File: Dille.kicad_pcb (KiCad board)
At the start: 2 copper layers, 44 x 94 mm, 71 parts, among them J1 Barrel_Jack_Switch, Q1 MMBFJ112, SW2 SW_DPDT_x2, U1 PT2399, U2 TL074, U3 L78L05_SOT89

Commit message: pcb
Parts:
- removed the R5 at (79.0, 85.0)
- removed the R5 at (240.2, 79.5)
- added R5: 15k, Resistor_SMD:R_0805_2012Metric_Pad1.20x1.40mm_HandSolder, F.Cu at (51.5, 104.5)
- C14, C19, C21, C25: footprint Capacitor_SMD:CP_Elec_4x5.4 -> Capacitor_SMD:CP_Elec_4x4.5
- C2: footprint Capacitor_SMD:CP_Elec_6.3x5.4 -> Capacitor_SMD:CP_Elec_6.3x4.5; moved to F.Cu
- C20: footprint Capacitor_SMD:CP_Elec_6.3x5.4 -> Capacitor_SMD:CP_Elec_6.3x4.5
- D3, E1, RV1, RV2, RV3, SW2: moved to B.Cu
- J1: footprint Connector_BarrelJack:BarrelJack_Horizontal -> Connector_BarrelJack:BarrelJack_Kycon_KLDX-0202-xC_Horizontal; moved to B.Cu
- R11: value 10k -> 100Ω
- R13: value 15k -> 10k
- R14: value 8.2k -> 1M
- R3: value 100Ω -> 10k
- R7: value 1M -> 8.2k
- TP1: value 9V -> GND; footprint TestPoint:TestPoint_THTPad_D2.5mm_Drill1.2mm -> TestPoint:Test point 2.5x1.5
- TP2, TP3, TP4: footprint TestPoint:TestPoint_THTPad_D2.5mm_Drill1.2mm -> TestPoint:Test point 2.5x1.5
- moved C22 191.3 mm to (55.0, 102.5), turned to 180 degrees
- moved C23 190.8 mm to (55.0, 100.0), turned to 180 degrees
- moved R23 190.6 mm to (50.0, 73.0), turned to 90 degrees
- moved C26 190.0 mm to (55.0, 89.0), turned to 180 degrees
- moved C21 181.3 mm to (60.8, 89.0)
- moved R27 176.4 mm to (64.5, 81.3), turned to 180 degrees
- moved R26 176.4 mm to (64.5, 78.9)
- moved C25 174.2 mm to (72.5, 66.0), turned to 90 degrees
- moved C20 172.8 mm to (51.8, 94.5), turned to -90 degrees
- moved C24 168.4 mm to (77.0, 73.8), turned to 180 degrees
- moved R25 163.5 mm to (77.0, 81.3)
- moved R24 163.5 mm to (77.0, 78.8), turned to 180 degrees
- moved R22 160.5 mm to (80.8, 64.2), turned to 180 degrees
- moved C9 155.6 mm to (51.5, 116.5)
- moved C8 155.1 mm to (51.5, 110.5)
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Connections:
- J1 pad 1: unconnected-(J1-Pad1) -> GND
- J1 pad 2: unconnected-(J1-Pad2) -> Net-(J1-Pad2)
- R1 pad 1: Net-(R1-Pad1) -> Net-(J1-Pad2)
- R11 pad 1: Net-(C8-Pad2) -> Net-(C6-Pad2)
- R11 pad 2: Net-(C9-Pad1) -> Net-(U2A-+)
- R13 pad 1: Net-(U1-LPF1-OUT) -> Net-(U2D--)
- R13 pad 2: Net-(C9-Pad1) -> Net-(Q1-D)
- R14 pad 1: Net-(C10-Pad2) -> +4V5
- R14 pad 2: Net-(C9-Pad1) -> Net-(C6-Pad2)
- R3 pad 1: Net-(C6-Pad2) -> Net-(C8-Pad2)
- R3 pad 2: Net-(U2A-+) -> Net-(C9-Pad1)
- R7 pad 1: +4V5 -> Net-(C10-Pad2)
- R7 pad 2: Net-(C6-Pad2) -> Net-(C9-Pad1)
- TP1 pad 1: Net-(R1-Pad1) -> GND
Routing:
- net +9V: track 0.00 -> 138.9 mm
- net Net-(U1-VCO): track 0.00 -> 86.2 mm, vias 0 -> 4
- net Net-(C13-Pad2): track 0.00 -> 50.0 mm, vias 0 -> 1
- net Net-(C9-Pad1): track 0.00 -> 48.7 mm
- net Net-(Q1-D): track 3.97 -> 45.4 mm, vias 0 -> 2
- net Net-(R15-Pad1): track 0.00 -> 41.2 mm, vias 0 -> 2
- net +4V5: track 0.00 -> 38.8 mm, vias 0 -> 2
- net +5V: track 0.00 -> 36.4 mm, vias 0 -> 2
- net Net-(C25-Pad2): track 0.00 -> 34.3 mm
- net Net-(C10-Pad2): track 0.00 -> 28.1 mm, vias 0 -> 2
- net Net-(U1-LPF1-OUT): track 0.00 -> 24.3 mm
- net Net-(U1-OP2-OUT): track 0.00 -> 20.6 mm
- net Net-(SW2A-B): track 0.00 -> 16.3 mm
- net Net-(U1-LPF2-OUT): track 0.00 -> 15.7 mm
- net Net-(U2A-+): track 0.00 -> 15.1 mm, vias 0 -> 2
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- added copper zone on B.Cu, net GND
- added copper zone on F.Cu, net GND
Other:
- board size 44 x 94 mm -> 44 x 95.5 mm
- board text added: "+ 9V -"
- board text added: "LED"

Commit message: pcb 2
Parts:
- moved R22 29.8 mm to (51.0, 63.2)
- moved RV2 27.9 mm to (83.0, 67.3)
- moved RV3 27.9 mm to (55.1, 67.3)
- moved R1 11.5 mm to (84.5, 58.0), turned to 180 degrees
- moved D1 11.1 mm to (84.5, 60.5), turned to 0 degrees
- moved R2 5.68 mm to (77.5, 58.0)
- moved C5 5.57 mm to (77.5, 63.0)
- moved R4 5.57 mm to (77.5, 60.5)
- moved R23 1.12 mm to (50.5, 74.0), turned to 180 degrees
- moved C13 0.50 mm to (84.0, 84.0), turned to 0 degrees
- moved R15 0.50 mm to (84.0, 86.5)
- moved R16 0.50 mm to (84.0, 89.0)
- moved TP2 0.22 mm to (88.0, 79.8)
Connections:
- net Net-(C25-Pad2) renamed Sig out
- net Net-(C6-Pad1) renamed Sig in
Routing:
- net Net-(U1-VCO): track 86.2 -> 54.4 mm, vias 4 -> 3
- net Net-(C13-Pad2): track 50.0 -> 29.2 mm, vias 1 -> 2
- net Net-(J1-Pad2): track 9.15 -> 21.4 mm
- net +4V5: track 38.8 -> 32.7 mm
- net +9V: track 138.9 -> 133.6 mm
- net Net-(C19-Pad2): track 13.2 -> 18.1 mm, vias 0 -> 1
- net Net-(R22-Pad2): track 8.17 -> 9.18 mm
- net Net-(R15-Pad1): track 41.2 -> 41.7 mm
- net GND: vias 25 -> 36

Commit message: Saddamointi
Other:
- board text added: "https://github.com/ Secret624/Dille"

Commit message: Added gerbers
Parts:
- added REF**: Pin_D0.7mm_L6.5mm_W1.8mm_FlatFork, Connector_Pin:Pin_D0.7mm_L6.5mm_W1.8mm_FlatFork, B.Cu at (36.0, 97.0)
- added REF**: Pin_D0.7mm_L6.5mm_W1.8mm_FlatFork, Connector_Pin:Pin_D0.7mm_L6.5mm_W1.8mm_FlatFork, B.Cu at (102.0, 97.0)
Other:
- board text added: "JLCJLCJLCJLC"

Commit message: Rev 2
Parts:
- moved R22 0.50 mm to (51.0, 63.8)
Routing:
- net Net-(SW2A-B): track 16.3 -> 17.6 mm
- net +9V: track 133.6 -> 132.8 mm
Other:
- board text added: "rev. 2"
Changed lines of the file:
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@@
   )
   (footprint "Resistor_SMD:R_0805_2012Metric_Pad1.20x1.40mm_HandSolder" (layer "F.Cu")
-    (at 51 63.25 180)
+    (at 51 63.75 180)
     (descr "Resistor SMD 0805 (2012 Metric), square (rectangular) end terminal, IPC_7351 nominal with elongated pad for handsoldering. (Body size source: IPC-SM-782 page 72, https://www.pcb-3d.com/wordpress/wp-content/uploads/ipc-sm-782a_amendment_1_and_2.pdf), generated with kicad-footprint-generator")
     (tags "resistor handsolder")
@@
     (fp_circle (center 0 0) (end 0 6.1)
       (stroke (width 0.1) (type default)) (fill none) (layer "Dwgs.User"))
-    (pad "1" thru_hole circle (at -6.05 7.1) (size 2.5 2.5) (drill 1.3) (layers "*.Cu" "*.Mask")
+    (pad "1" thru_hole oval (at -5.25 7.1) (size 5.5 3) (drill oval 4 1.5) (layers "*.Cu" "*.Mask")
       (net 3 "GND") (pinfunction "A") (pintype "passive"))
-    (pad "2" thru_hole circle (at -6.05 0) (size 2.5 2.5) (drill 1.3) (layers "*.Cu" "*.Mask")
+    (pad "2" thru_hole oval (at -5.25 0) (size 5.5 3) (drill oval 4 1.5) (layers "*.Cu" "*.Mask")
       (net 37 "Net-(SW2A-B)") (pinfunction "B") (pintype "passive"))
-    (pad "3" thru_hole circle (at -6.05 -7.1) (size 2.5 2.5) (drill 1.3) (layers "*.Cu" "*.Mask")
+    (pad "3" thru_hole oval (at -5.25 -7.1) (size 5.5 3) (drill oval 4 2) (layers "*.Cu" "*.Mask")
       (net 2 "+9V") (pinfunction "C") (pintype "passive"))
-    (pad "4" thru_hole circle (at 6.05 -7.1) (size 2.5 2.5) (drill 1.3) (layers "*.Cu" "*.Mask")
+    (pad "4" thru_hole oval (at 5.25 -7.1) (size 5.5 3) (drill oval 4 2) (layers "*.Cu" "*.Mask")
       (net 15 "unconnected-(SW2B-A-Pad4)") (pinfunction "A") (pintype "passive+no_connect"))
-    (pad "5" thru_hole circle (at 6.05 0) (size 2.5 2.5) (drill 1.3) (layers "*.Cu" "*.Mask")
+    (pad "5" thru_hole oval (at 5.25 0) (size 5.5 3) (drill oval 4 2) (layers "*.Cu" "*.Mask")
       (net 16 "unconnected-(SW2B-B-Pad5)") (pinfunction "B") (pintype "passive+no_connect"))
-    (pad "6" thru_hole circle (at 6.05 7.1) (size 2.5 2.5) (drill 1.3) (layers "*.Cu" "*.Mask")
+    (pad "6" thru_hole oval (at 5.25 7.1) (size 5.5 3) (drill oval 4 1.5) (layers "*.Cu" "*.Mask")
       (net 17 "unconnected-(SW2B-C-Pad6)") (pinfunction "C") (pintype "passive+no_connect"))
     (model "${KIPRJMOD}/stepsis/SF17010F-0302-21R-L.step"
@@
       (rotate (xyz 0 0 0))
     )
-    (model "${KIPRJMOD}/Resources/SF17010F-0302-21R-L.step"
-      (offset (xyz 0 0 3))
-      (scale (xyz 1 1 1))
-      (rotate (xyz 0 0 0))
-    )
-    (model "C:/Users/Uusi/Documents/KiCad/7.0/3dmodels/SF17010F-0302-21R-L.step"
-      (offset (xyz 0 0 3))
-      (scale (xyz 1 1 1))
-      (rotate (xyz 0 0 0))
-    )
   )
   (footprint "Potentiometer_THT:UT right angle long pin" (layer "B.Cu")
@@
     (effects (font (size 1 1) (thickness 0.16) bold) (justify left bottom))
   )
+  (gr_text "rev. 2" (at 49 62.5) (layer "F.SilkS")
+    (effects (font (size 1.5 1.5) (thickness 0.3) bold) (justify left bottom))
+  )
   (gr_text "LED" (at 69 108.5) (layer "F.SilkS")
     (effects (font (size 1 1) (thickness 0.15)))
@@
   (segment (start 70.75 78.171472) (end 69.078528 76.5) (width 0.5) (layer "F.Cu") (net 2))
   (segment (start 90 65) (end 90 98) (width 0.5) (layer "F.Cu") (net 2))
-  (segment (start 62.95 109.26) (end 64.94 111.25) (width 0.25) (layer "F.Cu") (net 2))
-  (segment (start 83.1 60.5) (end 83.1 58.15) (width 1) (layer "F.Cu") (net 2))
   (segment (start 80.5 108.5) (end 80.5 100) (width 0.25) (layer "F.Cu") (net 2))
+  (segment (start 83.1 60.5) (end 83.1 58.15) (width 1) (layer "F.Cu") (net 2))
+  (segment (start 63.75 109.26) (end 65.74 111.25) (width 0.25) (layer "F.Cu") (net 2))
   (segment (start 63.475 78.3475) (end 65.5125 76.31) (width 0.25) (layer "F.Cu") (net 2))
   (segment (start 69.078528 76.5) (end 68.525 76.5) (width 0.5) (layer "F.Cu") (net 2))
+  (segment (start 65.74 111.25) (end 77.75 111.25) (width 0.25) (layer "F.Cu") (net 2))
   (segment (start 72 82.75) (end 70.75 81.5) (width 0.5) (layer "F.Cu") (net 2))
   (segment (start 89 64) (end 90 65) (width 0.5) (layer "F.Cu") (net 2))
@@
   (segment (start 79.81 78.81) (end 77.975 78.81) (width 0.25) (layer "F.Cu") (net 2))
   (segment (start 68.525 76.5) (end 65.7025 76.5) (width 0.5) (layer "F.Cu") (net 2))
-  (segment (start 80.5 100) (end 82.5 100) (width 0.25) (layer "F.Cu") (net 2))
-  (segment (start 90 98) (end 88 100) (width 0.5) (layer "F.Cu") (net 2))
   (segment (start 77.75 111.25) (end 80.5 108.5) (width 0.25) (layer "F.Cu") (net 2))
-  (segment (start 64.94 111.25) (end 77.75 111.25) (width 0.25) (layer "F.Cu") (net 2))
+  (segment (start 90 98) (end 88 100) (width 0.5) (layer "F.Cu") (net 2))
+  (segment (start 80.5 100) (end 82.5 100) (width 0.25) (layer "F.Cu") (net 2))
   (via (at 79.25 80) (size 0.8) (drill 0.4) (layers "F.Cu" "B.Cu") (free) (net 3))
   (via (at 50 70.7) (size 0.8) (drill 0.4) (layers "F.Cu" "B.Cu") (free) (net 3))
@@
   (via (at 63.5 83) (size 0.8) (drill 0.4) (layers "F.Cu" "B.Cu") (free) (net 3))
   (via (at 52.5 101.25) (size 0.8) (drill 0.4) (layers "F.Cu" "B.Cu") (free) (net 3))
-  (via (at 52 61.25) (size 0.8) (drill 0.4) (layers "F.Cu" "B.Cu") (free) (net 3))
+  (via (at 53 61.5) (size 0.8) (drill 0.4) (layers "F.Cu" "B.Cu") (free) (net 3))
   (via (at 88 85.5) (size 0.8) (drill 0.4) (layers "F.Cu" "B.Cu") (free) (net 3))
   (via (at 78 84.25) (size 0.8) (drill 0.4) (layers "F.Cu" "B.Cu") (free) (net 3))
@@
   (segment (start 78.91 63.25) (end 83 67.34) (width 0.25) (layer "B.Cu") (net 35))
   (segment (start 65 105.5) (end 67.735 105.5) (width 0.25) (layer "F.Cu") (net 36))
-  (segment (start 62.81 116.5) (end 62.95 116.36) (width 0.25) (layer "F.Cu") (net 37))
-  (segment (start 63 105.5) (end 61 107.5) (width 0.25) (layer "F.Cu") (net 37))
+  (segment (start 61 111.5) (end 61 116.5) (width 0.25) (layer "F.Cu") (net 37))
+  (segment (start 61 116.5) (end 63.61 116.5) (width 0.25) (layer "F.Cu") (net 37))
+  (segment (start 63 105.5) (end 60.5 108) (width 0.25) (layer "F.Cu") (net 37))
+  (segment (start 60.5 108) (end 60.5 111) (width 0.25) (layer "F.Cu") (net 37))
+  (segment (start 63.61 116.5) (end 63.75 116.36) (width 0.25) (layer "F.Cu") (net 37))
   (segment (start 58.5 116.5) (end 60 116.5) (width 0.25) (layer "F.Cu") (net 37))
-  (segment (start 61 116.5) (end 62.81 116.5) (width 0.25) (layer "F.Cu") (net 37))
-  (segment (start 61 107.5) (end 61 116.5) (width 0.25) (layer "F.Cu") (net 37))
+  (segment (start 60.5 111) (end 61 111.5) (width 0.25) (layer "F.Cu") (net 37))
   (segment (start 61 116.5) (end 60 116.5) (width 0.25) (layer "F.Cu") (net 37))
   (segment (start 85 87.8) (end 85 87.5) (width 0.25) (layer "F.Cu") (net 38))

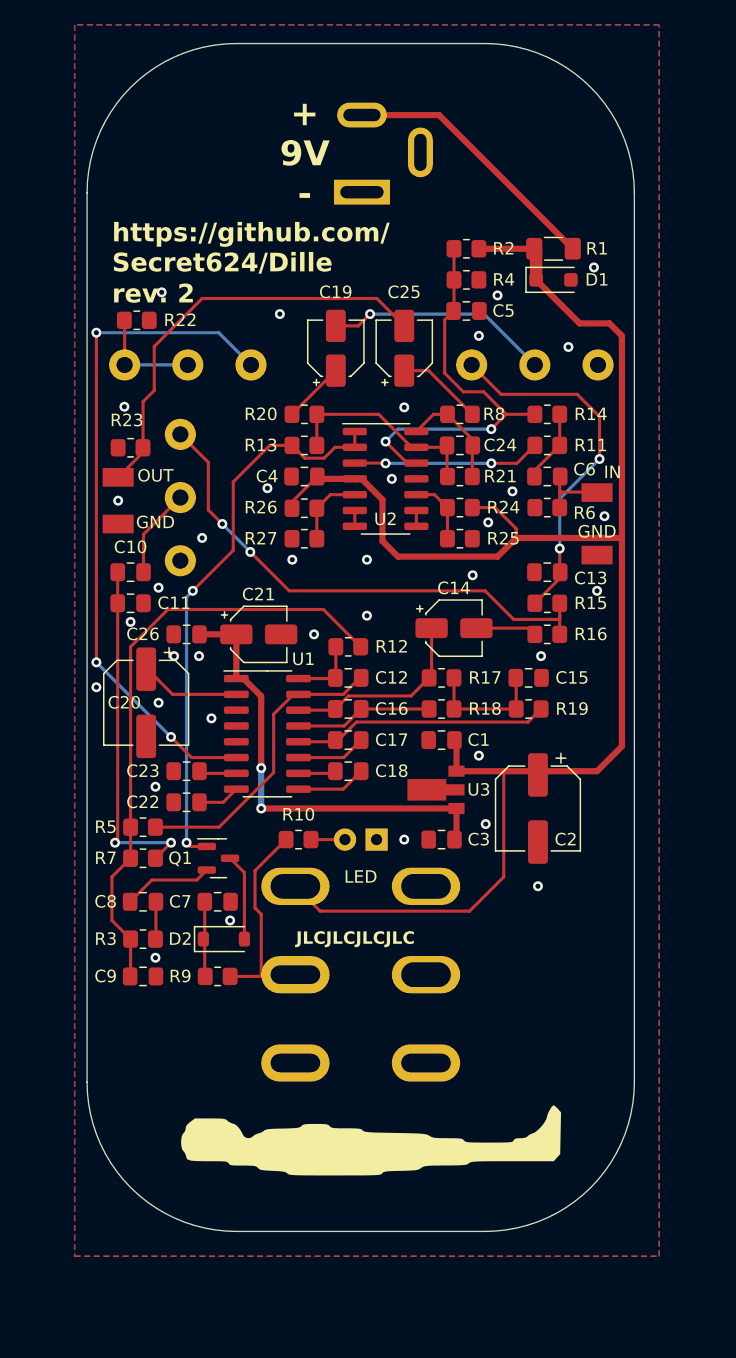
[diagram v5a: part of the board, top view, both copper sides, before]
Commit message: Silkscreen updated
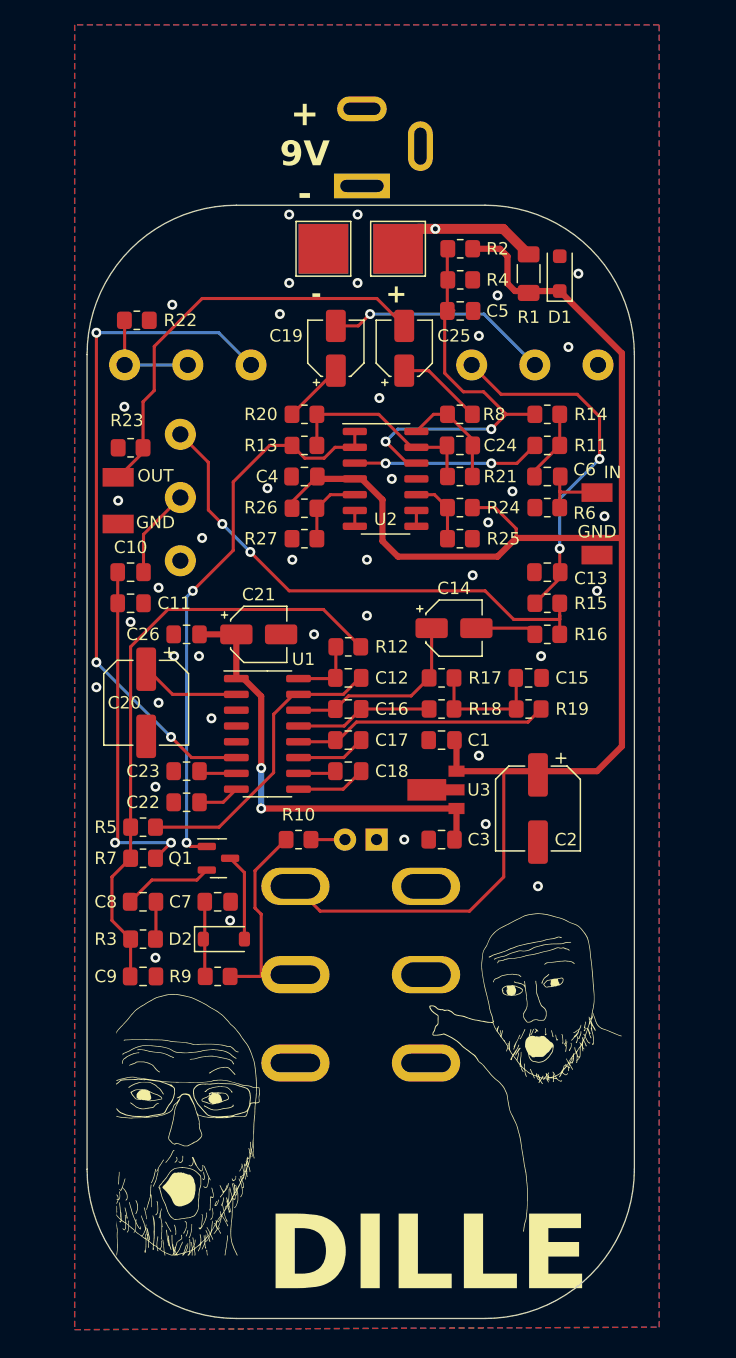
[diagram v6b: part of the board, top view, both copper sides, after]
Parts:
- added TP5: TestPoint, TestPoint:TestPoint_Pad_4.0x4.0mm, F.Cu at (72.0, 58.0)
- added TP5: TestPoint, TestPoint:TestPoint_Pad_4.0x4.0mm, B.Cu at (72.0, 58.0)
- added TP6: TestPoint, TestPoint:TestPoint_Pad_4.0x4.0mm, F.Cu at (66.0, 58.0)
- added TP6: TestPoint, TestPoint:TestPoint_Pad_4.0x4.0mm, B.Cu at (66.0, 58.0)
- moved R1 2.83 mm to (82.5, 60.0), turned to -90 degrees
- moved D1 0.71 mm to (85.0, 60.0), turned to 90 degrees
- moved C5 0.50 mm to (77.0, 63.0)
- moved J1 0.50 mm to (69.1, 53.0)
- moved R2 0.50 mm to (77.0, 58.0)
- moved R4 0.50 mm to (77.0, 60.5)
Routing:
- net Net-(J1-Pad2): track 21.4 -> 15.7 mm, vias 0 -> 1
- net +4V5: track 32.7 -> 31.8 mm
- net GND: vias 36 -> 40
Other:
- board size 44 x 95.5 mm -> 44 x 89.5 mm
- board text added: "+"
- board text added: "-"
- board text added: "DILLE"
- board text added: "SN:"
- board text removed: "LED"

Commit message: Revision 2
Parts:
- removed R24, R25, R26, R27: 100k, Resistor_SMD:R_0805_2012Metric_Pad1.20x1.40mm_HandSolder
- removed U2: TL074, Package_SO:SO-14_3.9x8.65mm_P1.27mm
- added U4: TL072, Package_SO:SO-8_3.9x4.9mm_P1.27mm, F.Cu at (71.0, 75.5)
- moved C4 9.71 mm to (72.6, 71.0)
- moved C24 2.24 mm to (77.0, 76.0)
- moved R13 2.24 mm to (64.5, 76.0), turned to 0 degrees
- moved R20 2.24 mm to (64.5, 73.5)
- moved R21 2.24 mm to (77.0, 78.5)
- moved R8 2.24 mm to (77.0, 73.5), turned to 180 degrees
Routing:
- net Net-(U2B-+): track 5.95 -> 0.00 mm
- net +9V: track 132.4 -> 126.9 mm, vias 0 -> 2
- net Net-(U2C-+): track 5.43 -> 0.00 mm
- net Net-(Q1-D): track 45.4 -> 41.5 mm
- net +4V5: track 31.8 -> 34.6 mm
- net Net-(U4A-+): track 15.1 -> 17.5 mm
- net Net-(C19-Pad1): track 4.98 -> 7.23 mm
- net Net-(U4B--): track 16.6 -> 18.5 mm
- net Net-(C25-Pad1): track 6.93 -> 8.34 mm
- net Net-(U2C--): track 1.27 -> 0.00 mm
- net Net-(U2B--): track 1.27 -> 0.00 mm
- net Net-(C24-Pad1): track 8.93 -> 9.51 mm
- net Net-(R22-Pad2): track 9.18 -> 8.68 mm
- net GND: vias 40 -> 39
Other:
- board text added: "locked"
- board text removed: "+ 9V -"
- board text removed: "https://github.com/ Secret624/Dille"
